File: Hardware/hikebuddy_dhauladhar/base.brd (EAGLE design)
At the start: 80 x 40.6 mm, 115 parts, among them J1 4P-SMD-2.0-90D, J2 4P-2.0-90D, U11 MF-DSC-SOT233-BSS84, U3 MF-DSC-SOT233-MMBT3904, U4 MF-DSC-SOT233-MMBT3904, U9 MF-DSC-SOT233-BSS84

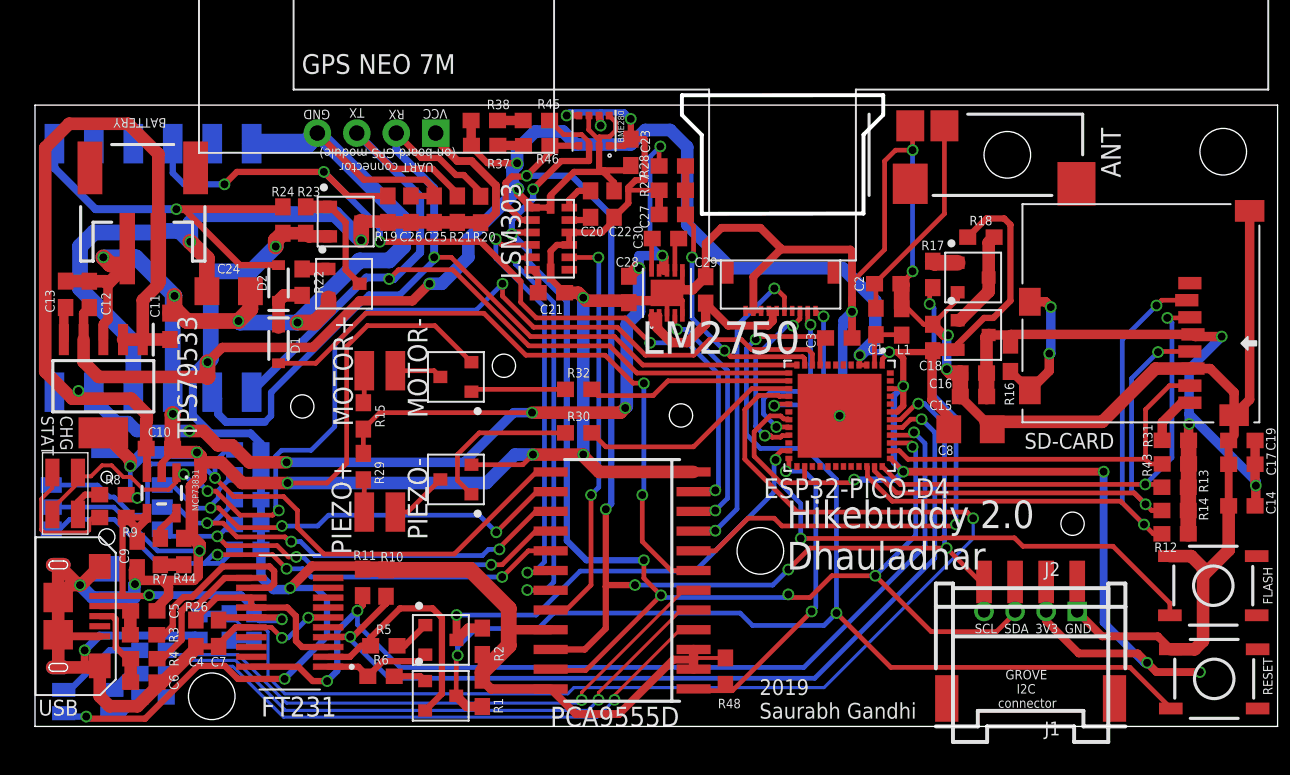
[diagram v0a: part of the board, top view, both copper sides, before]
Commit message: added 3D models for most PCB parts
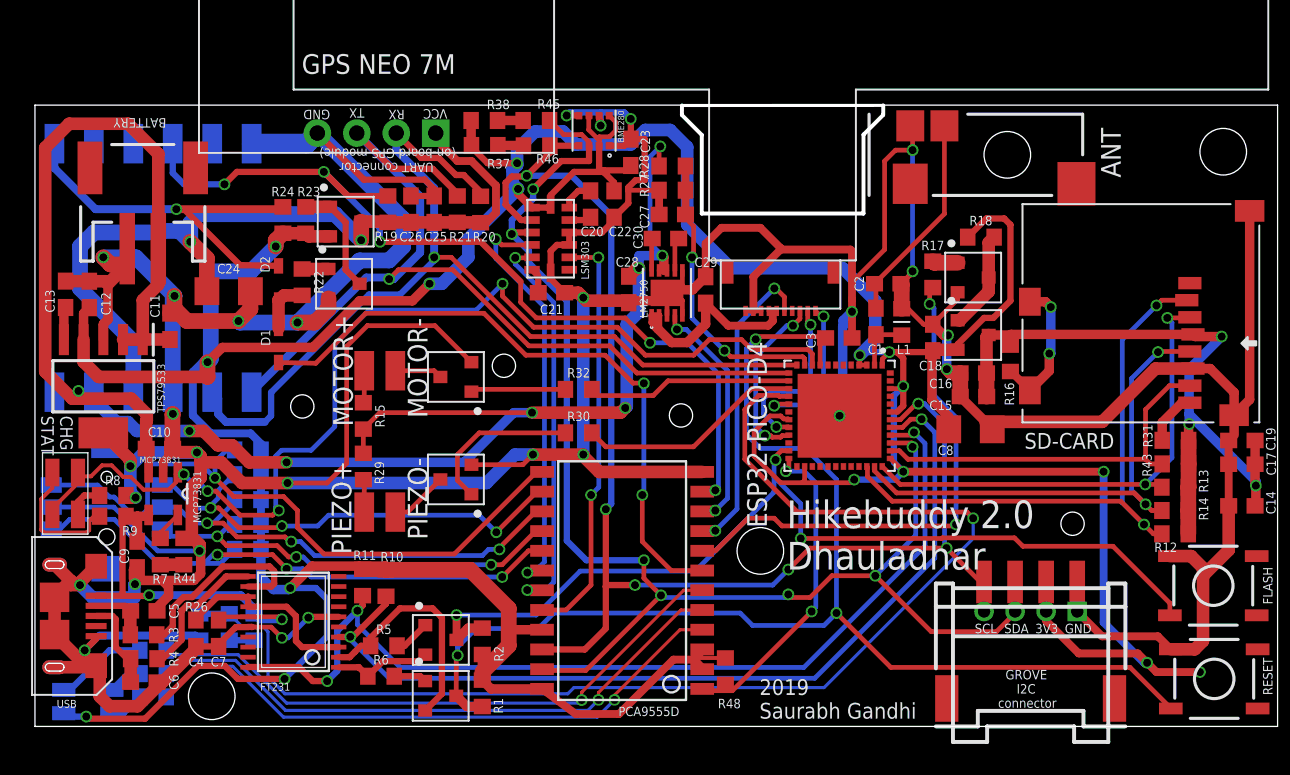
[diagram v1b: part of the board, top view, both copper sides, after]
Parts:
- removed USB: MF-CON-MICROUSB-RIGHT, MF_Connectors:MICROUSB-RIGHT
- added J3: MF-CON-MICROUSB-RIGHT, MF_Connectors:MICROUSB-RIGHT
- C1, C10, C11, C12, C13, C14, C15, C16, C17, C18, C19, C20, C21, C22, C23, C25, C26, C27, C30, C4, C5, C6: device SparkFun-Capacitors:0603 -> SparkFun-Capacitors:C0603
- C2: value 2.7pF -> 4.7pF; device SparkFun-Capacitors:0603 -> SparkFun-Capacitors:C0603
- C24, C8: value 4.7uF -> 10uF; device SparkFun-Capacitors:1206 -> SparkFun-Capacitors:C1206
- C28, C29, C7, C9: value 4.7uF -> 2.2uF; device SparkFun-Capacitors:0603 -> SparkFun-Capacitors:C0603
- C3: value 0.22uF -> 0.1uF; device SparkFun-Capacitors:0603 -> SparkFun-Capacitors:C0603
- D1, D2: device SparkFun-DiscreteSemi:SOD-323 -> SparkFun-DiscreteSemi:SOD323
- FLASH, RESET: value (none) -> MOMENTARY-SWITCH-SPST-SMD-5.2MM
- FT231: value FT231XS-U -> FT231XS-UTSSOP20; device FT231XS-U:SOP63P600X175-20N -> FT231XS-U:TSSOP20
- L1: value 1.6nH -> 30Ω/1.8A; device SparkFun-Coils:0603 -> SparkFun-Coils:L0603
- MCP73831: value MCP73831 -> MCP73831T-3ACI/OT; device SparkFun-IC-Power:SOT23-5 -> MCP73831T-3ACI_OT:SOT95P270X145-5N
- PCA9555D: value PCA9555D -> PCA9555; device PCA9555:SO24 -> PCA9555:SO24-2
- R1, R10, R11, R17, R18, R19, R2, R20, R21, R22, R23, R25, R26, R3, R30, R32, R33, R34, R35, R36, R37, R38, R39, R4, R40, R41, R42, R44, R45, R46, R47, R5, R6, R7, R8, R9: device SparkFun-Resistors:0603 -> SparkFun-Resistors:R0603
- R12, R13, R14, R31, R43: value 50k -> 10k; device SparkFun-Resistors:0603 -> SparkFun-Resistors:R0603
- R15, R29: value 27 -> 22; device SparkFun-Resistors:0603 -> SparkFun-Resistors:R0603
- R16: value 50k -> 330k; device SparkFun-Resistors:0603 -> SparkFun-Resistors:R0603
- R24: value 150k -> 47k; device SparkFun-Resistors:0603 -> SparkFun-Resistors:R0603
- R27, R28: value 150k -> 200k; device SparkFun-Resistors:0603 -> SparkFun-Resistors:R0603
- R48: value 10k -> 1k; device SparkFun-Resistors:0603 -> SparkFun-Resistors:R0603
- moved FT231 0.24 mm to (16.6, 6.73), turned to 90 degrees
- moved MCP73831 0.10 mm to (8.26, 15.0), turned to 270 degrees
- moved R9 0.08 mm to (5.01, 13.5)
- moved R8 0.05 mm to (5.01, 14.9)
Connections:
- net D+: now also J3.3; no longer USB.3
- net D-: now also J3.2; no longer USB.2
- net GND: now also J3.5, J3.S1, J3.S2, J3.S3, J3.S4, J3.S5, J3.S6; no longer USB.5, USB.S1, USB.S2, USB.S3, USB.S4, USB.S5, USB.S6
- net GPS_POWER: now also D1.2; no longer D1.A
- net N$16: now also D2.2; no longer D2.A
- net N$17: now also D1.1, D2.1; no longer D1.C, D2.C
- net V_USB: now also J3.1; no longer USB.1
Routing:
- net V_USB: track 26.5 -> 25.4 mm
- net N$5: track 11.8 -> 12.5 mm
- net ESP_TX: track 58.7 -> 58.0 mm
- net N$9: track 7.08 -> 6.40 mm
- net N$8: track 15.6 -> 14.9 mm
- net B4: track 43.8 -> 43.2 mm
- net GPS_POWER: track 41.0 -> 41.6 mm
- net SD_POWER: track 34.1 -> 33.5 mm
- net MAGDRDY: track 26.4 -> 27.0 mm
- net LED3: track 38.6 -> 39.1 mm
- net LED2: track 38.6 -> 39.2 mm
- net LED1: track 38.7 -> 39.2 mm
- net GPS_RESET: track 58.1 -> 57.6 mm
- net B5: track 37.4 -> 36.9 mm
- net B3: track 28.3 -> 27.7 mm
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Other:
- board size 80 x 40.6 mm -> 80 x 40 mm
- board text added: "FT231"
- board text added: "LM2750"
- board text added: "LSM303"
- board text added: "MCP73831"
- board text added: "TPS79533"
- board text added: "USB"

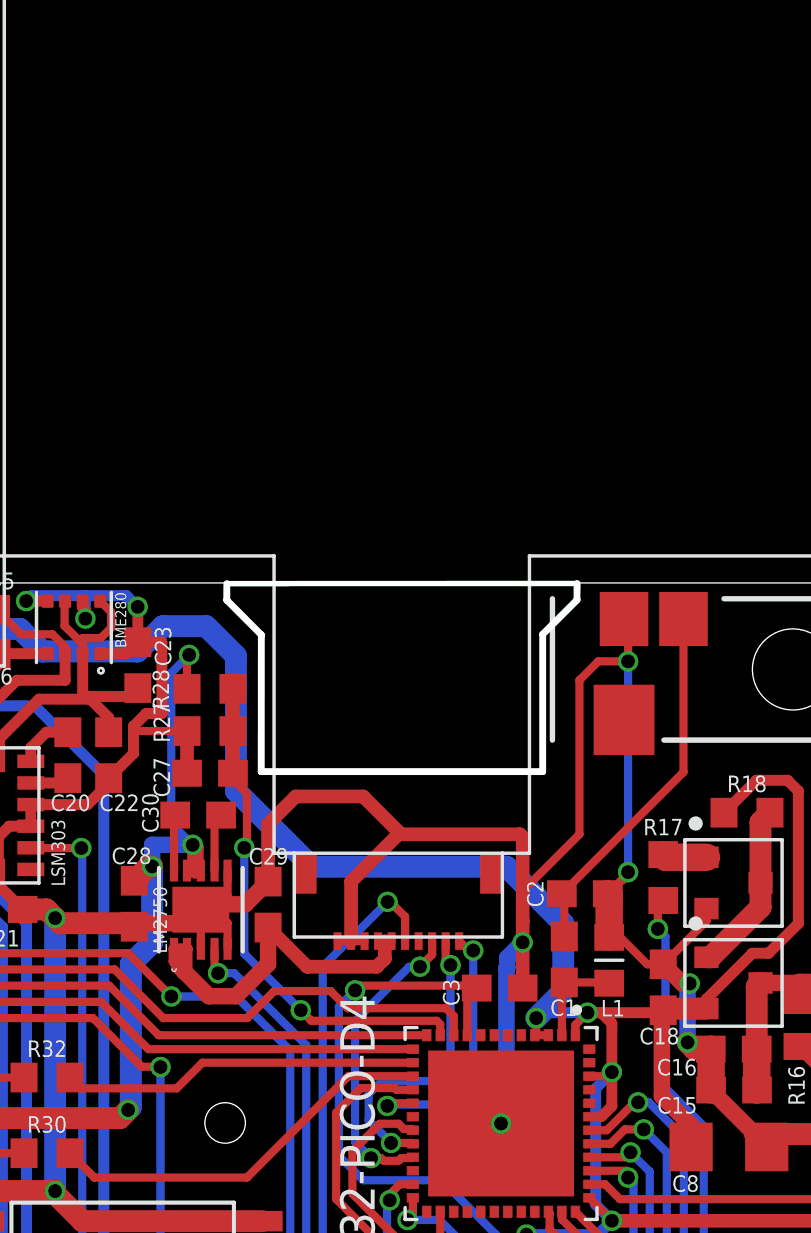
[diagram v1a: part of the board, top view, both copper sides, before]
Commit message: added lvgl submodule
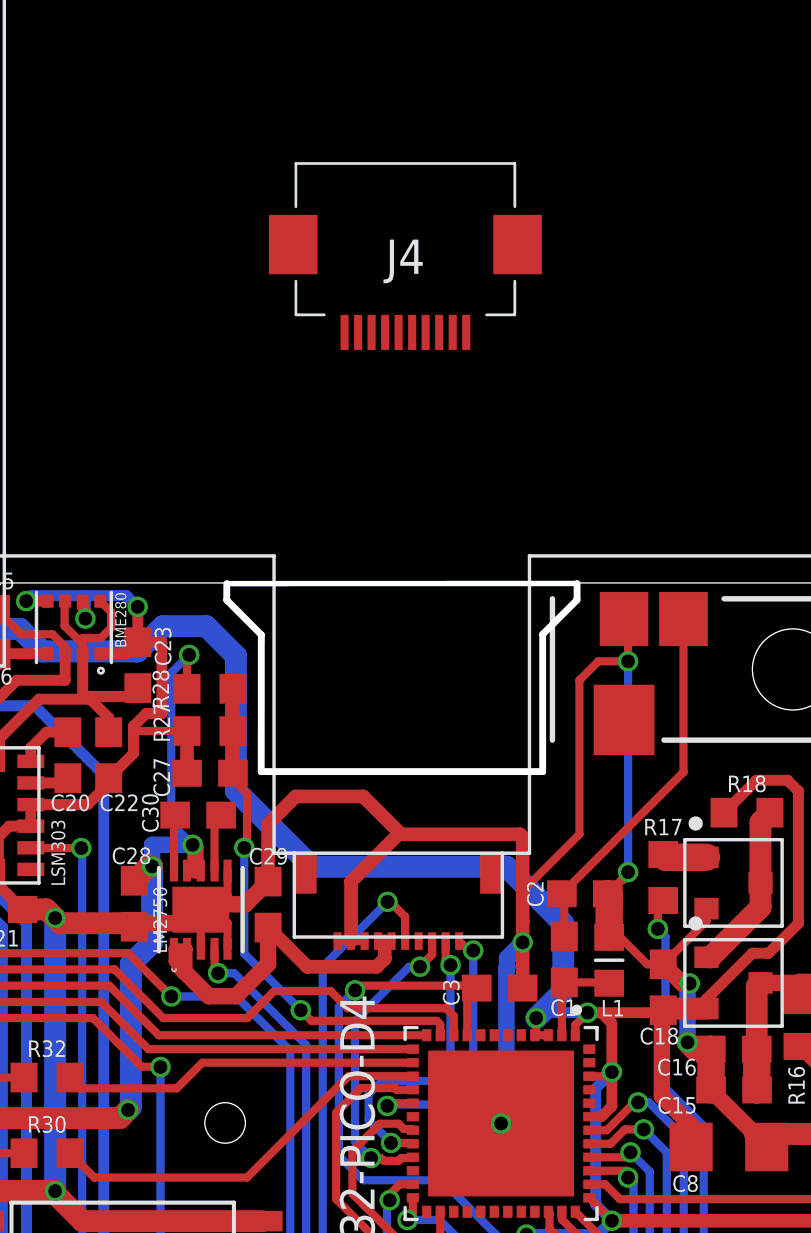
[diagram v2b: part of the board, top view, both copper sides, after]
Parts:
- added J4: FH12-10S-0.5SH(1)(98), FH12-10S-0.5SH(1)(98):FH1210S05SH198
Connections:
- new net N$40: J4.4
- net 5V: now also J4.6, J4.7
- net GND: now also J4.10, J4.11, J4.12, J4.8, J4.9
- net LCD_CLK: now also J4.1
- net LCD_CS: now also J4.3
- net LCD_DISPLAY: now also J4.5
- net LCD_MOSI: now also J4.2
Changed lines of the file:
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@@
 <?xml version="1.0" encoding="utf-8"?>
 <!DOCTYPE eagle SYSTEM "eagle.dtd">
-<eagle version="9.3.0">
+<eagle version="9.3.1">
 <drawing>
 <settings>
@@
 <setting verticaltext="up"/>
 </settings>
-<grid distance="0.1" unitdist="mm" unit="mm" style="lines" multiple="1" display="yes" altdistance="0.01" altunitdist="mm" altunit="mm"/>
+<grid distance="0.05" unitdist="inch" unit="inch" style="lines" multiple="1" display="yes" altdistance="0.005" altunitdist="inch" altunit="inch"/>
 <layers>
 <layer number="1" name="Top" color="4" fill="1" visible="yes" active="yes"/>
@@
 <layer number="23" name="tOrigins" color="15" fill="1" visible="yes" active="yes"/>
 <layer number="24" name="bOrigins" color="15" fill="1" visible="yes" active="yes"/>
-<layer number="25" name="tNames" color="7" fill="1" visible="yes" active="yes"/>
-<layer number="26" name="bNames" color="7" fill="1" visible="yes" active="yes"/>
-<layer number="27" name="tValues" color="7" fill="1" visible="yes" active="yes"/>
+<layer number="25" name="tNames" color="7" fill="1" visible="no" active="yes"/>
+<layer number="26" name="bNames" color="7" fill="1" visible="no" active="yes"/>
+<layer number="27" name="tValues" color="7" fill="1" visible="no" active="yes"/>
 <layer number="28" name="bValues" color="7" fill="1" visible="no" active="yes"/>
 <layer number="29" name="tStop" color="7" fill="3" visible="no" active="yes"/>
@@
 <layer number="37" name="tTest" color="7" fill="1" visible="no" active="yes"/>
 <layer number="38" name="bTest" color="7" fill="1" visible="no" active="yes"/>
-<layer number="39" name="tKeepout" color="4" fill="11" visible="yes" active="yes"/>
-<layer number="40" name="bKeepout" color="1" fill="11" visible="yes" active="yes"/>
-<layer number="41" name="tRestrict" color="4" fill="10" visible="yes" active="yes"/>
-<layer number="42" name="bRestrict" color="1" fill="10" visible="yes" active="yes"/>
-<layer number="43" name="vRestrict" color="2" fill="10" visible="yes" active="yes"/>
+<layer number="39" name="tKeepout" color="4" fill="11" visible="no" active="yes"/>
+<layer number="40" name="bKeepout" color="1" fill="11" visible="no" active="yes"/>
+<layer number="41" name="tRestrict" color="4" fill="10" visible="no" active="yes"/>
+<layer number="42" name="bRestrict" color="1" fill="10" visible="no" active="yes"/>
+<layer number="43" name="vRestrict" color="2" fill="10" visible="no" active="yes"/>
 <layer number="44" name="Drills" color="7" fill="1" visible="no" active="yes"/>
-<layer number="45" name="Holes" color="7" fill="1" visible="no" active="yes"/>
+<layer number="45" name="Holes" color="7" fill="1" visible="yes" active="yes"/>
 <layer number="46" name="Milling" color="3" fill="1" visible="no" active="yes"/>
 <layer number="47" name="Measures" color="7" fill="1" visible="no" active="yes"/>
@@
 <layer number="49" name="Reference" color="7" fill="1" visible="no" active="yes"/>
 <layer number="50" name="dxf" color="7" fill="1" visible="no" active="no"/>
-<layer number="51" name="tDocu" color="6" fill="1" visible="no" active="yes"/>
+<layer number="51" name="tDocu" color="6" fill="1" visible="yes" active="yes"/>
 <layer number="52" name="bDocu" color="7" fill="1" visible="no" active="yes"/>
 <layer number="53" name="tGND_GNDA" color="7" fill="9" visible="no" active="no"/>
@@
 <attribute name="POPULATE" value="1" x="2.667" y="7.112" size="1.778" layer="27" rot="R270" display="off"/>
 <attribute name="URL" value="https://factory.macrofab.com/part/MF-CON-MICROUSB-RIGHT" x="2.667" y="7.112" size="1.778" layer="27" rot="R270" display="off"/>
+</element>
+<element name="J4" library="FH12-10S-0.5SH(1)(98)" package="FH1210S05SH198" value="FH12-10S-0.5SH(1)(98)" x="48.26" y="52.07" smashed="yes" rot="R180">
+<attribute name="DESCRIPTION" value="FFC &amp; FPC Connectors 10P SMT HORIZONTAL .5MM PITCH" x="48.26" y="52.07" size="1.778" layer="27" font="vector" ratio="15" rot="R180" display="off"/>
+<attribute name="HEIGHT" value="2mm" x="48.26" y="52.07" size="1.778" layer="27" font="vector" ratio="15" rot="R180" display="off"/>
+<attribute name="MANUFACTURER_NAME" value="Hirose" x="48.26" y="52.07" size="1.778" layer="27" font="vector" ratio="15" rot="R180" display="off"/>
+<attribute name="MANUFACTURER_PART_NUMBER" value="FH12-10S-0.5SH(1)(98)" x="48.26" y="52.07" size="1.778" layer="27" font="vector" ratio="15" rot="R180" display="off"/>
+<attribute name="MOUSER_PART_NUMBER" value="798-FH1210S05SH198" x="48.26" y="52.07" size="1.778" layer="27" font="vector" ratio="15" rot="R180" display="off"/>
+<attribute name="MOUSER_PRICE-STOCK" value="https://www.mouser.com/Search/Refine.aspx?Keyword=798-FH1210S05SH198" x="48.26" y="52.07" size="1.778" layer="27" font="vector" ratio="15" rot="R180" display="off"/>
+<attribute name="NAME" x="48.26" y="52.07" size="1.27" layer="25" rot="R180" align="center"/>
+<attribute name="RS_PART_NUMBER" value="" x="48.26" y="52.07" size="1.778" layer="27" font="vector" ratio="15" rot="R180" display="off"/>
+<attribute name="RS_PRICE-STOCK" value="" x="48.26" y="52.07" size="1.778" layer="27" font="vector" ratio="15" rot="R180" display="off"/>
+<attribute name="VALUE" x="48.26" y="52.07" size="1.27" layer="27" rot="R180" align="center"/>
 </element>
 </elements>
@@
 <wire x1="8.255" y1="16.3576" x2="8.255" y2="17.055" width="0.508" layer="1"/>
 <wire x1="8.255" y1="17.055" x2="8.86" y2="17.66" width="0.508" layer="1"/>
+<contactref element="J4" pad="11"/>
+<contactref element="J4" pad="12"/>
+<contactref element="J4" pad="8"/>
+<contactref element="J4" pad="10"/>
+<contactref element="J4" pad="9"/>
+<wire x1="47.01" y1="49.27" x2="52.41" y2="52.52" width="0" layer="19" extent="1-1"/>
+<wire x1="46.51" y1="49.27" x2="47.01" y2="49.27" width="0" layer="19" extent="1-1"/>
+<wire x1="46.01" y1="49.27" x2="46.51" y2="49.27" width="0" layer="19" extent="1-1"/>
+<wire x1="44.11" y1="52.52" x2="46.01" y2="49.27" width="0" layer="19" extent="1-1"/>
+<wire x1="6.6" y1="1.3" x2="47.01" y2="49.27" width="0" layer="19" extent="1-1"/>
 </signal>
 <signal name="N$1">
@@
 <wire x1="40.182" y1="25.682" x2="40.1" y2="25.6" width="0.4064" layer="1"/>
 <wire x1="40.182" y1="26.4622" x2="39.6994" y2="26.4622" width="0.4064" layer="1"/>
+<contactref element="J4" pad="6"/>
+<contactref element="J4" pad="7"/>
+<wire x1="47.51" y1="49.27" x2="39.6994" y2="26.0006" width="0" layer="19" extent="1-1"/>
+<wire x1="48.01" y1="49.27" x2="47.51" y2="49.27" width="0" layer="19" extent="1-1"/>
 </signal>
 <signal name="NC2">
@@
 <wire x1="49.93" y1="25.87" x2="49.75" y2="26.05" width="0.3048" layer="1"/>
 <via x="49.93" y="25.86" extent="1-16" drill="0.508"/>
-<wire x1="49.93" y1="25.86" x2="49.93" y2="23.3" width="0.3048" layer="16"/>
-<wire x1="49.93" y1="23.3" x2="49.93" y2="22.0872375" width="0.3048" layer="16"/>
+<wire x1="49.93" y1="25.86" x2="49.93" y2="22.0872375" width="0.3048" layer="16"/>
 <wire x1="47.38645" y1="21.5704" x2="46.8996" y2="21.08355" width="0.3048" layer="16"/>
 <wire x1="46.8996" y1="21.08355" x2="46.8996" y2="20.1204" width="0.3048" layer="16"/>
@@
 <wire x1="48.535" y1="19.25" x2="48.505" y2="19.28" width="0.3048" layer="1"/>
 <wire x1="48.505" y1="19.28" x2="47.73" y2="19.28" width="0.3048" layer="1"/>
+<contactref element="J4" pad="2"/>
+<wire x1="50.01" y1="49.27" x2="46.8996" y2="20.1204" width="0" layer="19" extent="1-16"/>
 </signal>
 <signal name="LCD_CLK">
@@
 <wire x1="50.25" y1="26.75" x2="50.6" y2="26.4" width="0.3048" layer="1"/>
 <wire x1="50.6" y1="26.4" x2="50.77" y2="26.4" width="0.3048" layer="1"/>
+<contactref element="J4" pad="1"/>
+<wire x1="50.51" y1="49.27" x2="47.59" y2="20.65" width="0" layer="19" extent="1-1"/>
 </signal>
 <signal name="LCD_CS">
@@
 <wire x1="47.45645" y1="18.6196" x2="47.35605" y2="18.72" width="0.3048" layer="1"/>
 <wire x1="47.35605" y1="18.72" x2="46.99" y2="18.72" width="0.3048" layer="1"/>
+<contactref element="J4" pad="3"/>
+<wire x1="49.51" y1="49.27" x2="46.4" y2="19.31" width="0" layer="19" extent="1-16"/>
 </signal>
 <signal name="GPIO_INT">
@@
 <wire x1="42.425" y1="12.6" x2="42.9562" y2="12.575" width="0.3048" layer="1"/>
 <wire x1="45.2" y1="25.8" x2="45.2" y2="14" width="0.3048" layer="16"/>
+<contactref element="J4" pad="5"/>
+<wire x1="48.51" y1="49.27" x2="42.425" y2="12.6" width="0" layer="19" extent="1-1"/>
 </signal>
 <signal name="USB_DETECT">
@@
 <wire x1="6" y1="3.4" x2="6.76" y2="3.4" width="0.4064" layer="16"/>
 </signal>
+<signal name="N$40">
+<contactref element="J4" pad="4"/>
+</signal>
 </signals>
